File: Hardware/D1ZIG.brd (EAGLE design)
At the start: 33.6 x 25.4 mm, 5 parts

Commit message: Final DRC and tweaks for v1.0 release
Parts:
- renumbered J3 to J1, J4 to J2
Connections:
- removed net RX: J2.2
- removed net TX: J2.1

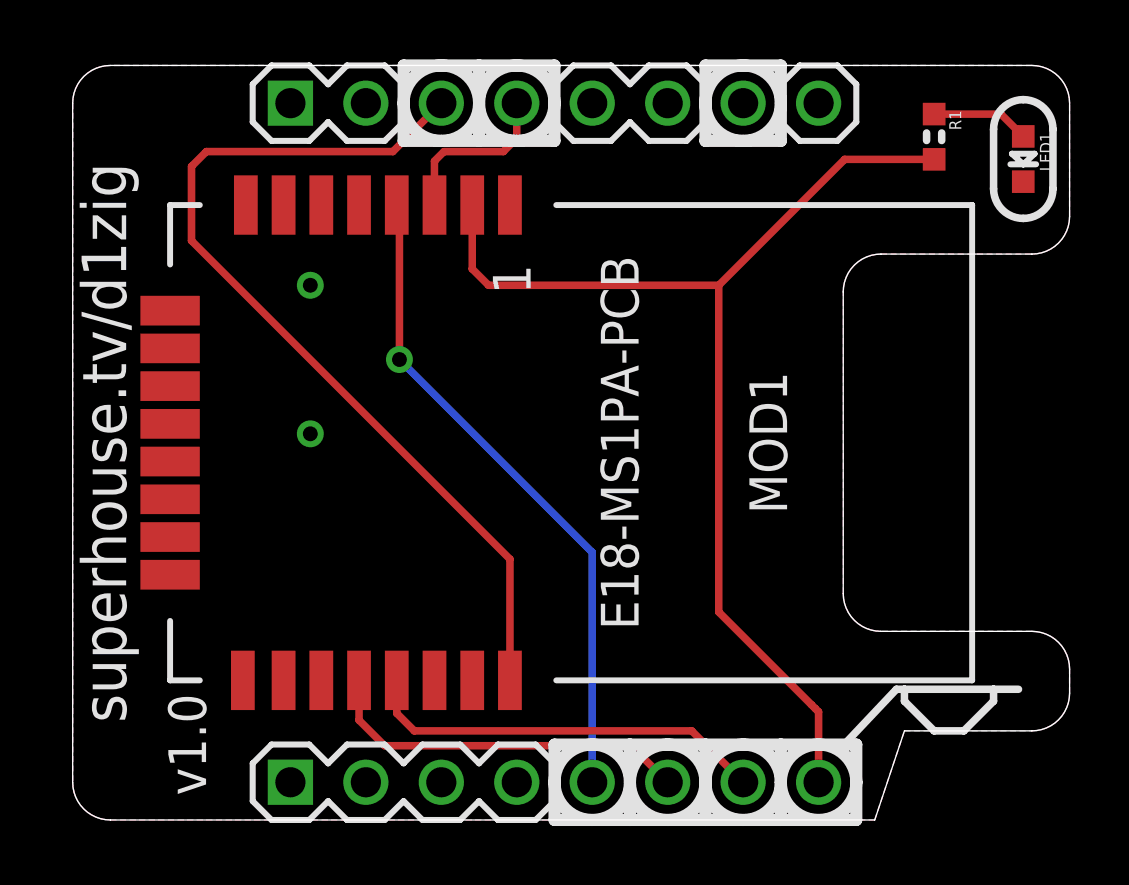
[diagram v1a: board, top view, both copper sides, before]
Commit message: Flipped entire board for reverse mounting on D1 Mini for v1.0 release
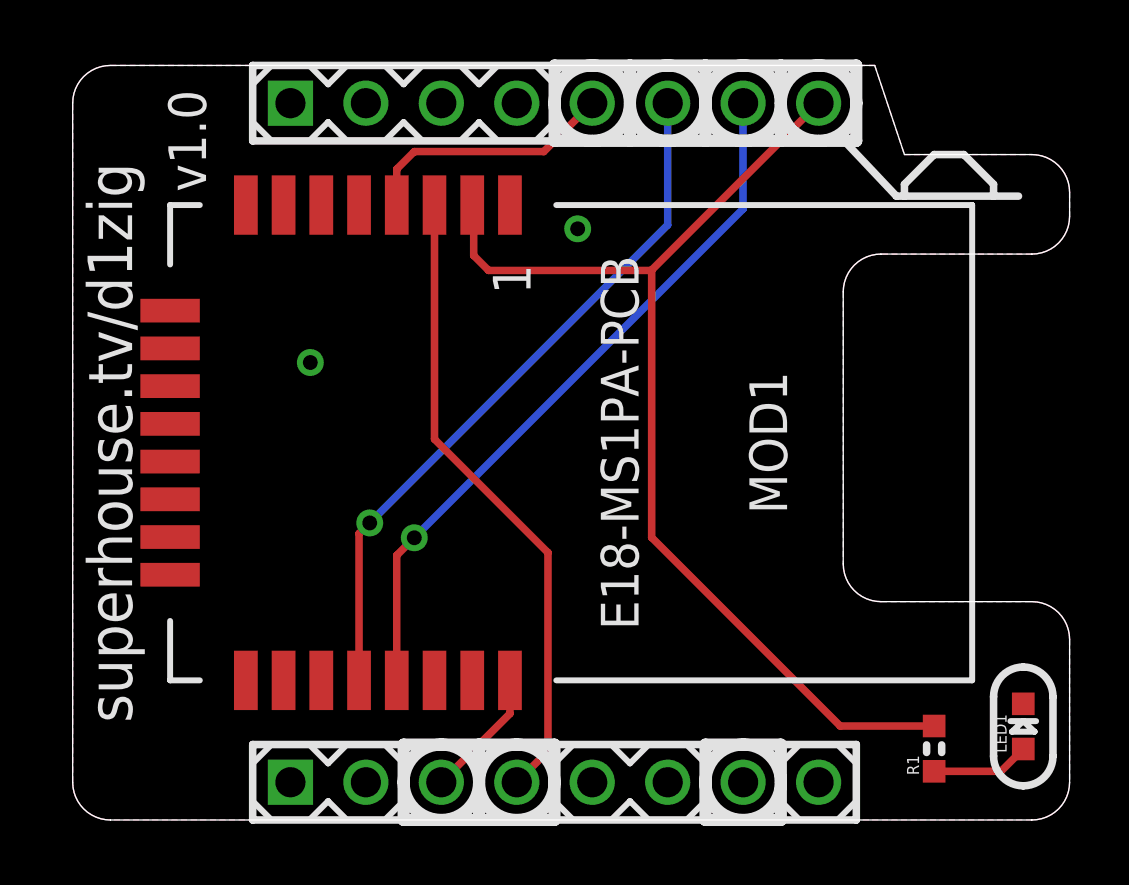
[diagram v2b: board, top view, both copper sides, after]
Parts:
- R1: value 2K2 -> 4K7
- moved J1 22.9 mm to (7.33, 24.1)
- moved J2 22.9 mm to (7.33, 1.27)
- moved R1 20.6 mm to (29.0, 2.40), turned to 90 degrees
- moved LED1 19.1 mm to (32.0, 3.15), turned to 90 degrees
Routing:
- net D1_CC_RST: track 31.0 -> 4.39 mm
- net D2_P2_2_DC: track 5.75 -> 21.4 mm
- net D6_P2_1_DD: track 22.2 -> 8.71 mm, vias 1 -> 0
- net D7_P0_3: track 12.6 -> 23.7 mm, vias 0 -> 1
- net D8_P0_2: track 13.7 -> 24.3 mm, vias 0 -> 1
- net 3.3V: track 37.8 -> 37.0 mm
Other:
- outline, holes or cut-outs redrawn
